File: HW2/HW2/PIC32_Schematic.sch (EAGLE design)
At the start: 22 parts

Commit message: Schematic is connected further
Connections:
- removed net N$16: U$2.13.VDD
- removed net N$17: U$2.12.RA4
- removed net N$18: U$2.11.RB4
- removed net N$21: U$2.8.VSS
- removed net N$22: U$2.7.RB3
- removed net N$23: U$2.6.RB2
- removed net N$26: U$2.3.RA1
- removed net N$27: U$2.2.RA0
- new net A0: J2.8, U$2.2.RA0
- new net A1: J2.7, U$2.3.RA1
- new net A4: J2.3, U$2.12.RA4
- new net B2: J2.6, U$2.6.RB2
- new net B3: J2.5, U$2.7.RB3
- new net B4: J2.4, U$2.11.RB4
- net +3V3: now also C2.1, J2.2, U$2.13.VDD
- net GND: now also C2.2, J2.1, U$2.8.VSS
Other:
- moved on the sheet: C2, J1, J2, J3
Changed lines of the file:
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@@
 <instance part="U$6" gate="G$1" x="85.09" y="-22.86"/>
 <instance part="U$7" gate="G$1" x="-99.06" y="-38.1"/>
-<instance part="J1" gate="G$1" x="-87.63" y="3.81"/>
-<instance part="J2" gate="G$1" x="74.93" y="34.29"/>
-<instance part="J3" gate="G$1" x="96.52" y="34.29"/>
+<instance part="J1" gate="G$1" x="-90.17" y="49.53"/>
+<instance part="J2" gate="G$1" x="-60.96" y="0"/>
+<instance part="J3" gate="G$1" x="46.99" y="1.27" rot="R180"/>
 <instance part="LED1" gate="G$1" x="100.33" y="-1.27"/>
 <instance part="LED2" gate="G$1" x="99.06" y="11.43"/>
@@
 <instance part="R4" gate="G$1" x="105.41" y="-33.02"/>
 <instance part="C1" gate="G$1" x="21.59" y="27.94" rot="R270"/>
-<instance part="C2" gate="G$1" x="119.38" y="6.35"/>
+<instance part="C2" gate="G$1" x="-19.05" y="-27.94" rot="R270"/>
 <instance part="C3" gate="G$1" x="119.38" y="-6.35"/>
 <instance part="C4" gate="G$1" x="119.38" y="-17.78"/>
@@
 <instance part="+3V1" gate="G$1" x="24.13" y="35.56"/>
 <instance part="P+1" gate="1" x="-36.83" y="44.45"/>
-<instance part="GND1" gate="1" x="33.02" y="20.32"/>
+<instance part="GND1" gate="1" x="-25.4" y="-30.48"/>
 </instances>
 <busses>
@@
 </segment>
 </net>
-<net name="N$16" class="0">
-<segment>
-<pinref part="U$2" gate="G$1" pin="13.VDD"/>
-<wire x1="-15.24" y1="-27.94" x2="-16.51" y2="-27.94" width="0.1524" layer="91"/>
-</segment>
-</net>
-<net name="N$17" class="0">
-<segment>
-<pinref part="U$2" gate="G$1" pin="12.RA4"/>
-<wire x1="-15.24" y1="-22.86" x2="-16.51" y2="-22.86" width="0.1524" layer="91"/>
-</segment>
-</net>
-<net name="N$18" class="0">
-<segment>
-<pinref part="U$2" gate="G$1" pin="11.RB4"/>
-<wire x1="-15.24" y1="-17.78" x2="-16.51" y2="-17.78" width="0.1524" layer="91"/>
-</segment>
-</net>
 <net name="N$19" class="0">
 <segment>
@@
 </segment>
 </net>
-<net name="N$21" class="0">
-<segment>
-<pinref part="U$2" gate="G$1" pin="8.VSS"/>
-<wire x1="-15.24" y1="-2.54" x2="-16.51" y2="-2.54" width="0.1524" layer="91"/>
-</segment>
-</net>
-<net name="N$22" class="0">
-<segment>
-<pinref part="U$2" gate="G$1" pin="7.RB3"/>
-<wire x1="-15.24" y1="2.54" x2="-16.51" y2="2.54" width="0.1524" layer="91"/>
-</segment>
-</net>
-<net name="N$23" class="0">
-<segment>
-<pinref part="U$2" gate="G$1" pin="6.RB2"/>
-<wire x1="-15.24" y1="7.62" x2="-16.51" y2="7.62" width="0.1524" layer="91"/>
-</segment>
-</net>
 <net name="N$24" class="0">
 <segment>
@@
 </segment>
 </net>
-<net name="N$26" class="0">
+<net name="A1" class="0">
 <segment>
 <pinref part="U$2" gate="G$1" pin="3.RA1"/>
 <wire x1="-15.24" y1="22.86" x2="-16.51" y2="22.86" width="0.1524" layer="91"/>
-</segment>
-</net>
-<net name="N$27" class="0">
-<segment>
-<pinref part="U$2" gate="G$1" pin="2.RA0"/>
-<wire x1="-15.24" y1="27.94" x2="-16.51" y2="27.94" width="0.1524" layer="91"/>
+<label x="-19.05" y="22.86" size="1.778" layer="95"/>
+</segment>
+<segment>
+<pinref part="J2" gate="G$1" pin="7"/>
+<wire x1="-55.88" y1="7.62" x2="-54.61" y2="7.62" width="0.1524" layer="91"/>
+<label x="-54.61" y="7.62" size="1.778" layer="95"/>
 </segment>
 </net>
@@
 <label x="16.51" y="7.62" size="1.778" layer="95"/>
 </segment>
+<segment>
+<pinref part="J2" gate="G$1" pin="2"/>
+<wire x1="-55.88" y1="-5.08" x2="-54.61" y2="-5.08" width="0.1524" layer="91"/>
+<label x="-54.61" y="-5.08" size="1.778" layer="95"/>
+</segment>
+<segment>
+<pinref part="U$2" gate="G$1" pin="13.VDD"/>
+<wire x1="-15.24" y1="-27.94" x2="-16.51" y2="-27.94" width="0.1524" layer="91"/>
+<label x="-22.86" y="-27.94" size="1.778" layer="95"/>
+<pinref part="C2" gate="G$1" pin="1"/>
+</segment>
 </net>
 <net name="GND" class="0">
 <segment>
 <pinref part="U$2" gate="G$1" pin="19.VSS"/>
-<label x="16.51" y="-12.7" size="1.778" layer="95"/>
+<label x="16.51" y="-15.24" size="1.778" layer="95"/>
 <wire x1="15.24" y1="-12.7" x2="24.13" y2="-12.7" width="0.1524" layer="91"/>
 <pinref part="C5" gate="G$1" pin="-"/>
@@
 <label x="-27.94" y="-10.16" size="1.778" layer="95"/>
 </segment>
-</net>
+<segment>
+<pinref part="J2" gate="G$1" pin="1"/>
+<wire x1="-55.88" y1="-7.62" x2="-54.61" y2="-7.62" width="0.1524" layer="91"/>
+<label x="-54.61" y="-7.62" size="1.778" layer="95"/>
+</segment>
+<segment>
+<pinref part="U$2" gate="G$1" pin="8.VSS"/>
+<wire x1="-15.24" y1="-2.54" x2="-16.51" y2="-2.54" width="0.1524" layer="91"/>
+<label x="-21.59" y="-2.54" size="1.778" layer="95"/>
+</segment>
+<segment>
+<pinref part="C2" gate="G$1" pin="2"/>
+<pinref part="GND1" gate="1" pin="GND"/>
+<wire x1="-25.4" y1="-27.94" x2="-24.13" y2="-27.94" width="0.1524" layer="91"/>
+</segment>
+</net>
+<net name="A0" class="0">
+<segment>
+<pinref part="J2" gate="G$1" pin="8"/>
+<wire x1="-55.88" y1="10.16" x2="-54.61" y2="10.16" width="0.1524" layer="91"/>
+<label x="-54.61" y="10.16" size="1.778" layer="95"/>
+</segment>
+<segment>
+<pinref part="U$2" gate="G$1" pin="2.RA0"/>
+<wire x1="-15.24" y1="27.94" x2="-16.51" y2="27.94" width="0.1524" layer="91"/>
+<label x="-19.05" y="27.94" size="1.778" layer="95"/>
+</segment>
+</net>
+<net name="B2" class="0">
+<segment>
+<pinref part="J2" gate="G$1" pin="6"/>
+<wire x1="-55.88" y1="5.08" x2="-54.61" y2="5.08" width="0.1524" layer="91"/>
+<label x="-54.61" y="5.08" size="1.778" layer="95"/>
+</segment>
+<segment>
+<pinref part="U$2" gate="G$1" pin="6.RB2"/>
+<wire x1="-15.24" y1="7.62" x2="-16.51" y2="7.62" width="0.1524" layer="91"/>
+<label x="-19.05" y="7.62" size="1.778" layer="95"/>
+</segment>
+</net>
+<net name="B3" class="0">
+<segment>
+<pinref part="J2" gate="G$1" pin="5"/>
+<wire x1="-55.88" y1="2.54" x2="-54.61" y2="2.54" width="0.1524" layer="91"/>
+<label x="-54.61" y="2.54" size="1.778" layer="95"/>
+</segment>
+<segment>
+<pinref part="U$2" gate="G$1" pin="7.RB3"/>
+<wire x1="-15.24" y1="2.54" x2="-16.51" y2="2.54" width="0.1524" layer="91"/>
+<label x="-19.05" y="2.54" size="1.778" layer="95"/>
+</segment>
+</net>
+<net name="B4" class="0">
+<segment>
+<pinref part="J2" gate="G$1" pin="4"/>
+<wire x1="-55.88" y1="0" x2="-54.61" y2="0" width="0.1524" layer="91"/>
+<label x="-54.61" y="0" size="1.778" layer="95"/>
+</segment>
+<segment>
+<pinref part="U$2" gate="G$1" pin="11.RB4"/>
+<wire x1="-15.24" y1="-17.78" x2="-16.51" y2="-17.78" width="0.1524" layer="91"/>
+<label x="-19.05" y="-17.78" size="1.778" layer="95"/>
+</segment>
+</net>
+<net name="A4" class="0">
+<segment>
+<pinref part="J2" gate="G$1" pin="3"/>
+<wire x1="-55.88" y1="-2.54" x2="-54.61" y2="-2.54" width="0.1524" layer="91"/>
+<label x="-54.61" y="-2.54" size="1.778" layer="95"/>
+</segment>
+<segment>
+<pinref part="U$2" gate="G$1" pin="12.RA4"/>
+<wire x1="-15.24" y1="-22.86" x2="-16.51" y2="-22.86" width="0.1524" layer="91"/>
+<label x="-19.05" y="-22.86" size="1.778" layer="95"/>
+</segment>
+</net>

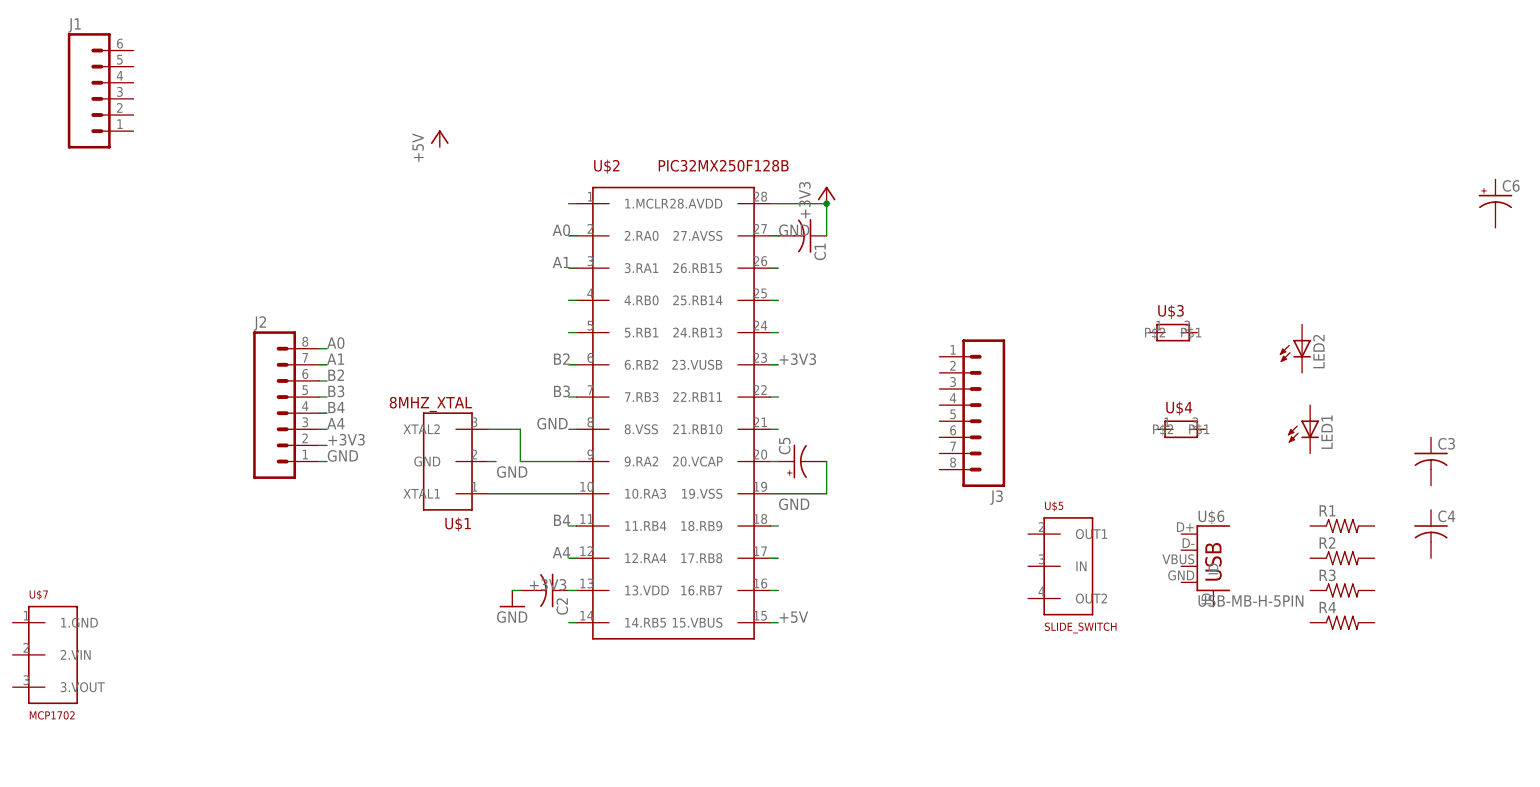
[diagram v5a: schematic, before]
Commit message: Pins 1-13 connected
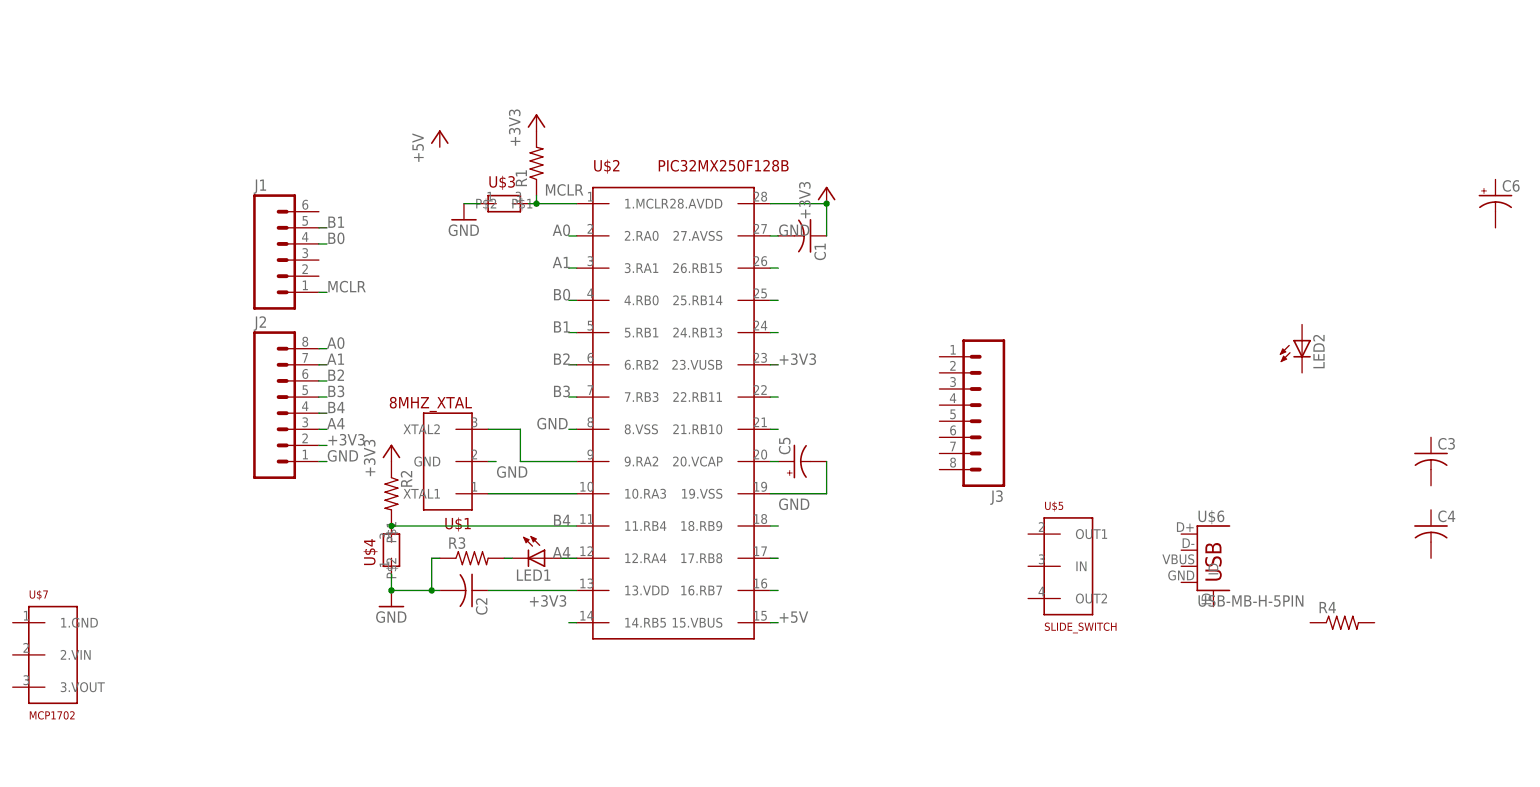
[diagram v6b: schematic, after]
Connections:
- removed net N$24: U$2.5.RB1
- removed net N$25: U$2.4.RB0
- removed net N$28: U$2.1.MCLR
- new net B0: J1.4, U$2.4.RB0
- new net B1: J1.5, U$2.5.RB1
- new net MCLR: J1.1, R1.1, U$2.1.MCLR, U$3.P$2
- new net N$1: LED1.C, R3.2
- net +3V3: now also R1.2, R2.1
- net A4: now also LED1.A
- net B4: now also R2.2, U$4.P$2
- net GND: now also R3.1, U$3.P$1, U$4.P$1
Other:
- moved on the sheet: C2, J1, LED1, R1, R2, R3, U$3, U$4
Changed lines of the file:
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@@
 <part name="+3V1" library="ME433" deviceset="+3V3" device=""/>
 <part name="P+1" library="ME433" deviceset="+5V" device=""/>
-<part name="GND1" library="ME433" deviceset="GND" device=""/>
+<part name="GND2" library="ME433" deviceset="GND" device=""/>
+<part name="+3V2" library="ME433" deviceset="+3V3" device=""/>
+<part name="GND3" library="ME433" deviceset="GND" device=""/>
+<part name="+3V3" library="ME433" deviceset="+3V3" device=""/>
 </parts>
 <sheets>
@@
 <instance part="U$1" gate="G$1" x="-29.21" y="-2.54" rot="R180"/>
 <instance part="U$2" gate="G$1" x="0" y="0"/>
-<instance part="U$3" gate="G$1" x="78.74" y="12.7"/>
-<instance part="U$4" gate="G$1" x="80.01" y="-2.54"/>
+<instance part="U$3" gate="G$1" x="-26.67" y="33.02"/>
+<instance part="U$4" gate="G$1" x="-44.45" y="-21.59" rot="R90"/>
 <instance part="U$5" gate="G$1" x="63.5" y="-24.13"/>
 <instance part="U$6" gate="G$1" x="85.09" y="-22.86"/>
 <instance part="U$7" gate="G$1" x="-99.06" y="-38.1"/>
-<instance part="J1" gate="G$1" x="-90.17" y="49.53"/>
+<instance part="J1" gate="G$1" x="-60.96" y="24.13"/>
 <instance part="J2" gate="G$1" x="-60.96" y="0"/>
 <instance part="J3" gate="G$1" x="46.99" y="1.27" rot="R180"/>
-<instance part="LED1" gate="G$1" x="100.33" y="-1.27"/>
+<instance part="LED1" gate="G$1" x="-20.32" y="-22.86" rot="R270"/>
 <instance part="LED2" gate="G$1" x="99.06" y="11.43"/>
-<instance part="R1" gate="G$1" x="105.41" y="-17.78"/>
-<instance part="R2" gate="G$1" x="105.41" y="-22.86"/>
-<instance part="R3" gate="G$1" x="105.41" y="-27.94"/>
+<instance part="R1" gate="G$1" x="-21.59" y="39.37" rot="R90"/>
+<instance part="R2" gate="G$1" x="-44.45" y="-12.7" rot="R270"/>
+<instance part="R3" gate="G$1" x="-31.75" y="-22.86"/>
 <instance part="R4" gate="G$1" x="105.41" y="-33.02"/>
 <instance part="C1" gate="G$1" x="21.59" y="27.94" rot="R270"/>
-<instance part="C2" gate="G$1" x="-19.05" y="-27.94" rot="R270"/>
+<instance part="C2" gate="G$1" x="-31.75" y="-27.94" rot="R270"/>
 <instance part="C3" gate="G$1" x="119.38" y="-6.35"/>
 <instance part="C4" gate="G$1" x="119.38" y="-17.78"/>
@@
 <instance part="+3V1" gate="G$1" x="24.13" y="35.56"/>
 <instance part="P+1" gate="1" x="-36.83" y="44.45"/>
-<instance part="GND1" gate="1" x="-25.4" y="-30.48"/>
+<instance part="GND2" gate="1" x="-33.02" y="30.48"/>
+<instance part="+3V2" gate="G$1" x="-21.59" y="46.99"/>
+<instance part="GND3" gate="1" x="-44.45" y="-30.48"/>
+<instance part="+3V3" gate="G$1" x="-44.45" y="-5.08"/>
 </instances>
 <busses>
@@
 </segment>
 </net>
-<net name="N$24" class="0">
-<segment>
-<pinref part="U$2" gate="G$1" pin="5.RB1"/>
-<wire x1="-15.24" y1="12.7" x2="-16.51" y2="12.7" width="0.1524" layer="91"/>
-</segment>
-</net>
-<net name="N$25" class="0">
-<segment>
-<pinref part="U$2" gate="G$1" pin="4.RB0"/>
-<wire x1="-15.24" y1="17.78" x2="-16.51" y2="17.78" width="0.1524" layer="91"/>
-</segment>
-</net>
 <net name="A1" class="0">
 <segment>
@@
 </segment>
 </net>
-<net name="N$28" class="0">
+<net name="MCLR" class="0">
 <segment>
 <pinref part="U$2" gate="G$1" pin="1.MCLR"/>
-<wire x1="-15.24" y1="33.02" x2="-16.51" y2="33.02" width="0.1524" layer="91"/>
+<wire x1="-15.24" y1="33.02" x2="-21.59" y2="33.02" width="0.1524" layer="91"/>
+<pinref part="U$3" gate="G$1" pin="P$2"/>
+<label x="-20.32" y="34.29" size="1.778" layer="95"/>
+<wire x1="-21.59" y1="33.02" x2="-22.86" y2="33.02" width="0.1524" layer="91"/>
+<wire x1="-21.59" y1="33.02" x2="-21.59" y2="34.29" width="0.1524" layer="91"/>
+<junction x="-21.59" y="33.02"/>
+<pinref part="R1" gate="G$1" pin="1"/>
+</segment>
+<segment>
+<pinref part="J1" gate="G$1" pin="1"/>
+<wire x1="-55.88" y1="19.05" x2="-54.61" y2="19.05" width="0.1524" layer="91"/>
+<label x="-54.61" y="19.05" size="1.778" layer="95"/>
 </segment>
 </net>
@@
 </segment>
 <segment>
+<pinref part="R1" gate="G$1" pin="2"/>
+<pinref part="+3V2" gate="G$1" pin="+3V3"/>
+</segment>
+<segment>
+<pinref part="R2" gate="G$1" pin="1"/>
+<pinref part="+3V3" gate="G$1" pin="+3V3"/>
+</segment>
+<segment>
 <pinref part="U$2" gate="G$1" pin="13.VDD"/>
-<wire x1="-15.24" y1="-27.94" x2="-16.51" y2="-27.94" width="0.1524" layer="91"/>
-<label x="-22.86" y="-27.94" size="1.778" layer="95"/>
 <pinref part="C2" gate="G$1" pin="1"/>
+<wire x1="-29.21" y1="-27.94" x2="-15.24" y2="-27.94" width="0.1524" layer="91"/>
+<label x="-22.86" y="-30.48" size="1.778" layer="95"/>
 </segment>
 </net>
@@
 </segment>
 <segment>
+<pinref part="U$3" gate="G$1" pin="P$1"/>
+<wire x1="-30.48" y1="33.02" x2="-33.02" y2="33.02" width="0.1524" layer="91"/>
+<pinref part="GND2" gate="1" pin="GND"/>
+</segment>
+<segment>
+<pinref part="U$4" gate="G$1" pin="P$1"/>
+<pinref part="GND3" gate="1" pin="GND"/>
+<wire x1="-44.45" y1="-27.94" x2="-44.45" y2="-25.4" width="0.1524" layer="91"/>
 <pinref part="C2" gate="G$1" pin="2"/>
-<pinref part="GND1" gate="1" pin="GND"/>
-<wire x1="-25.4" y1="-27.94" x2="-24.13" y2="-27.94" width="0.1524" layer="91"/>
+<wire x1="-44.45" y1="-27.94" x2="-38.1" y2="-27.94" width="0.1524" layer="91"/>
+<junction x="-44.45" y="-27.94"/>
+<pinref part="R3" gate="G$1" pin="1"/>
+<wire x1="-38.1" y1="-27.94" x2="-36.83" y2="-27.94" width="0.1524" layer="91"/>
+<wire x1="-36.83" y1="-22.86" x2="-38.1" y2="-22.86" width="0.1524" layer="91"/>
+<wire x1="-38.1" y1="-22.86" x2="-38.1" y2="-27.94" width="0.1524" layer="91"/>
+<junction x="-38.1" y="-27.94"/>
 </segment>
 </net>
@@
 </segment>
 <segment>
+<pinref part="U$4" gate="G$1" pin="P$2"/>
+<pinref part="R2" gate="G$1" pin="2"/>
 <pinref part="U$2" gate="G$1" pin="11.RB4"/>
-<wire x1="-15.24" y1="-17.78" x2="-16.51" y2="-17.78" width="0.1524" layer="91"/>
+<wire x1="-44.45" y1="-17.78" x2="-15.24" y2="-17.78" width="0.1524" layer="91"/>
+<junction x="-44.45" y="-17.78"/>
 <label x="-19.05" y="-17.78" size="1.778" layer="95"/>
 </segment>
@@
 <segment>
 <pinref part="U$2" gate="G$1" pin="12.RA4"/>
-<wire x1="-15.24" y1="-22.86" x2="-16.51" y2="-22.86" width="0.1524" layer="91"/>
+<wire x1="-15.24" y1="-22.86" x2="-17.78" y2="-22.86" width="0.1524" layer="91"/>
 <label x="-19.05" y="-22.86" size="1.778" layer="95"/>
-</segment>
-</net>
+<pinref part="LED1" gate="G$1" pin="A"/>
+</segment>
+</net>
+<net name="B0" class="0">
+<segment>
+<pinref part="J1" gate="G$1" pin="4"/>
+<wire x1="-55.88" y1="26.67" x2="-54.61" y2="26.67" width="0.1524" layer="91"/>
+<label x="-54.61" y="26.67" size="1.778" layer="95"/>
+</segment>
+<segment>
+<pinref part="U$2" gate="G$1" pin="4.RB0"/>
+<wire x1="-15.24" y1="17.78" x2="-16.51" y2="17.78" width="0.1524" layer="91"/>
+<label x="-19.05" y="17.78" size="1.778" layer="95"/>
+</segment>
+</net>
+<net name="B1" class="0">
+<segment>
+<pinref part="J1" gate="G$1" pin="5"/>
+<wire x1="-55.88" y1="29.21" x2="-54.61" y2="29.21" width="0.1524" layer="91"/>
+<label x="-54.61" y="29.21" size="1.778" layer="95"/>
+</segment>
+<segment>
+<pinref part="U$2" gate="G$1" pin="5.RB1"/>
+<wire x1="-15.24" y1="12.7" x2="-16.51" y2="12.7" width="0.1524" layer="91"/>
+<label x="-19.05" y="12.7" size="1.778" layer="95"/>
+</segment>
+</net>
+<net name="N$1" class="0">
+<segment>
+<pinref part="LED1" gate="G$1" pin="C"/>
+<pinref part="R3" gate="G$1" pin="2"/>
+<wire x1="-26.67" y1="-22.86" x2="-25.4" y2="-22.86" width="0.1524" layer="91"/>
+</segment>
+</net>
